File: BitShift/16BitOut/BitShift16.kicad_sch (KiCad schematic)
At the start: 7 parts, among them U1 74AHC595, U2 74AHC595

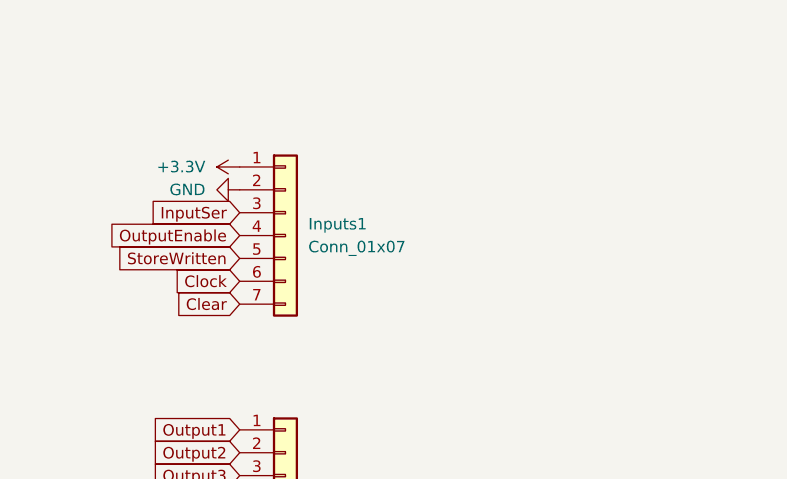
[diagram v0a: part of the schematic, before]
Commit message: renamed components
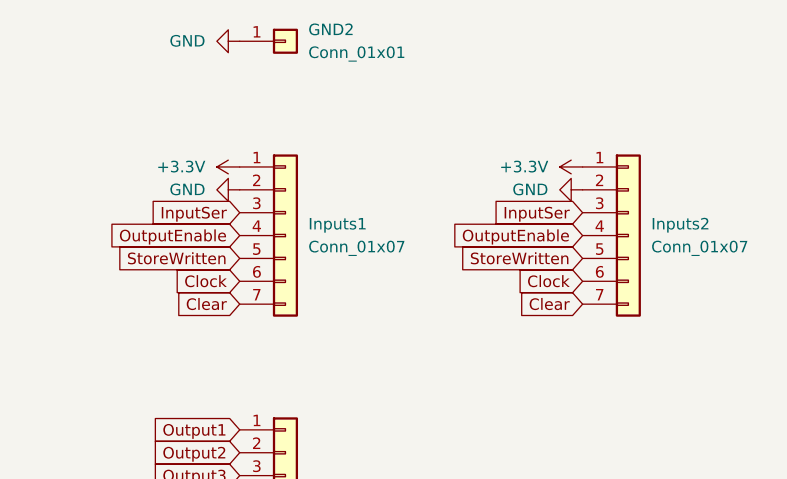
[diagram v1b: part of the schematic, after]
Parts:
- added GND2: Conn_01x01, Connector_PinHeader_2.54mm:PinHeader_1x01_P2.54mm_Vertical, symbol Connector_Generic:Conn_01x01
- added Inputs2: Conn_01x07, Connector_JST:JST_EH_S7B-EH_1x07_P2.50mm_Horizontal, symbol Connector_Generic:Conn_01x07
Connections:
- net +3.3V: now also Inputs2.1 (Pin_1)
- net Clear: now also Inputs2.7 (Pin_7)
- net Clock: now also Inputs2.6 (Pin_6)
- net GND: now also GND2.1 (Pin_1), Inputs2.2 (Pin_2)
- net InputSer: now also Inputs2.3 (Pin_3)
- net OutputEnable: now also Inputs2.4 (Pin_4)
- net StoreWritten: now also Inputs2.5 (Pin_5)
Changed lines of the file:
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@@
+    )
+  )
+  (global_label "Clear" (shape input) (at 257.81 86.36 180) (fields_autoplaced)
+    (effects (font (size 1.27 1.27)) (justify right))
+    (property "Intersheetrefs" "${INTERSHEET_REFS}" (at 249.8658 86.36 0)
+      (effects (font (size 1.27 1.27)) (justify right) hide)
     )
   )
@@
     )
   )
+  (global_label "Clock" (shape input) (at 257.81 83.82 180) (fields_autoplaced)
+    (effects (font (size 1.27 1.27)) (justify right))
+    (property "Intersheetrefs" "${INTERSHEET_REFS}" (at 249.6239 83.82 0)
+      (effects (font (size 1.27 1.27)) (justify right) hide)
+    )
+  )
   (global_label "Clock" (shape input) (at 219.71 83.82 180) (fields_autoplaced)
     (effects (font (size 1.27 1.27)) (justify right))
@@
     )
   )
+  (global_label "InputSer" (shape input) (at 257.81 76.2 180) (fields_autoplaced)
+    (effects (font (size 1.27 1.27)) (justify right))
+    (property "Intersheetrefs" "${INTERSHEET_REFS}" (at 246.963 76.2 0)
+      (effects (font (size 1.27 1.27)) (justify right) hide)
+    )
+  )
   (global_label "Output10" (shape input) (at 158.75 140.97 0) (fields_autoplaced)
     (effects (font (size 1.27 1.27)) (justify left))
@@
     )
   )
+  (global_label "StoreWritten" (shape input) (at 257.81 81.28 180) (fields_autoplaced)
+    (effects (font (size 1.27 1.27)) (justify right))
+    (property "Intersheetrefs" "${INTERSHEET_REFS}" (at 243.3344 81.28 0)
+      (effects (font (size 1.27 1.27)) (justify right) hide)
+    )
+  )
   (global_label "Clear" (shape input) (at 121.92 85.09 180) (fields_autoplaced)
     (effects (font (size 1.27 1.27)) (justify right))
@@
     (property "Intersheetrefs" "${INTERSHEET_REFS}" (at 169.1736 85.09 0)
       (effects (font (size 1.27 1.27)) (justify left) hide)
+    )
+  )
+  (global_label "OutputEnable" (shape input) (at 257.81 78.74 180) (fields_autoplaced)
+    (effects (font (size 1.27 1.27)) (justify right))
+    (property "Intersheetrefs" "${INTERSHEET_REFS}" (at 242.2461 78.74 0)
+      (effects (font (size 1.27 1.27)) (justify right) hide)
     )
   )
@@
         (path "/33c18695-af67-4dec-a71b-72e9af012bd4"
           (reference "#PWR03") (unit 1)
+        )
+      )
+    )
+  )
+  (symbol (lib_id "Connector_Generic:Conn_01x07") (at 262.89 78.74 0) (unit 1)
+    (in_bom yes) (on_board yes) (dnp no) (fields_autoplaced)
+    (property "Reference" "Inputs2" (at 265.43 77.47 0)
+      (effects (font (size 1.27 1.27)) (justify left))
+    )
+    (property "Value" "Conn_01x07" (at 265.43 80.01 0)
+      (effects (font (size 1.27 1.27)) (justify left))
+    )
+    (property "Footprint" "Connector_JST:JST_EH_S7B-EH_1x07_P2.50mm_Horizontal" (at 262.89 78.74 0)
+      (effects (font (size 1.27 1.27)) hide)
+    )
+    (property "Datasheet" "~" (at 262.89 78.74 0)
+      (effects (font (size 1.27 1.27)) hide)
+    )
+    (pin "6")
+    (pin "4")
+    (pin "7")
+    (pin "1")
+    (pin "3")
+    (pin "5")
+    (pin "2")
+    (instances
+      (project "MultiBitShift"
+        (path "/33c18695-af67-4dec-a71b-72e9af012bd4"
+          (reference "Inputs2") (unit 1)
         )
       )
@@
         (path "/33c18695-af67-4dec-a71b-72e9af012bd4"
           (reference "Outputs1") (unit 1)
+        )
+      )
+    )
+  )
+  (symbol (lib_id "power:+3.3V") (at 257.81 71.12 90) (unit 1)
+    (in_bom yes) (on_board yes) (dnp no) (fields_autoplaced)
+    (property "Reference" "#PWR08" (at 261.62 71.12 0)
+      (effects (font (size 1.27 1.27)) hide)
+    )
+    (property "Value" "+3.3V" (at 254 71.12 90)
+      (effects (font (size 1.27 1.27)) (justify left))
+    )
+    (property "Footprint" "" (at 257.81 71.12 0)
+      (effects (font (size 1.27 1.27)) hide)
+    )
+    (property "Datasheet" "" (at 257.81 71.12 0)
+      (effects (font (size 1.27 1.27)) hide)
+    )
+    (pin "1")
+    (instances
+      (project "MultiBitShift"
+        (path "/33c18695-af67-4dec-a71b-72e9af012bd4"
+          (reference "#PWR08") (unit 1)
+        )
+      )
+    )
+  )
+  (symbol (lib_id "power:GND") (at 219.71 57.15 270) (unit 1)
+    (in_bom yes) (on_board yes) (dnp no) (fields_autoplaced)
+    (property "Reference" "#PWR07" (at 213.36 57.15 0)
+      (effects (font (size 1.27 1.27)) hide)
+    )
+    (property "Value" "GND" (at 215.9 57.15 90)
+      (effects (font (size 1.27 1.27)) (justify right))
+    )
+    (property "Footprint" "" (at 219.71 57.15 0)
+      (effects (font (size 1.27 1.27)) hide)
+    )
+    (property "Datasheet" "" (at 219.71 57.15 0)
+      (effects (font (size 1.27 1.27)) hide)
+    )
+    (pin "1")
+    (instances
+      (project "MultiBitShift"
+        (path "/33c18695-af67-4dec-a71b-72e9af012bd4"
+          (reference "#PWR07") (unit 1)
+        )
+      )
+    )
+  )
+  (symbol (lib_id "power:GND") (at 257.81 73.66 270) (unit 1)
+    (in_bom yes) (on_board yes) (dnp no) (fields_autoplaced)
+    (property "Reference" "#PWR09" (at 251.46 73.66 0)
+      (effects (font (size 1.27 1.27)) hide)
+    )
+    (property "Value" "GND" (at 254 73.66 90)
+      (effects (font (size 1.27 1.27)) (justify right))
+    )
+    (property "Footprint" "" (at 257.81 73.66 0)
+      (effects (font (size 1.27 1.27)) hide)
+    )
+    (property "Datasheet" "" (at 257.81 73.66 0)
+      (effects (font (size 1.27 1.27)) hide)
+    )
+    (pin "1")
+    (instances
+      (project "MultiBitShift"
+        (path "/33c18695-af67-4dec-a71b-72e9af012bd4"
+          (reference "#PWR09") (unit 1)
         )
       )
@@
         )
       )
+    )
+  )
+  (symbol (lib_id "Connector_Generic:Conn_01x01") (at 224.79 57.15 0) (unit 1)
+    (in_bom yes) (on_board yes) (dnp no) (fields_autoplaced)
+    (property "Reference" "GND2" (at 227.33 55.88 0)
+      (effects (font (size 1.27 1.27)) (justify left))
+    )
+    (property "Value" "Conn_01x01" (at 227.33 58.42 0)
+      (effects (font (size 1.27 1.27)) (justify left))
+    )
+    (property "Footprint" "Connector_PinHeader_2.54mm:PinHeader_1x01_P2.54mm_Vertical" (at 224.79 57.15 0)
+      (effects (font (size 1.27 1.27)) hide)
+    )
+    (property "Datasheet" "~" (at 224.79 57.15 0)
+      (effects (font (size 1.27 1.27)) hide)
+    )
+    (pin "1")
+    (instances
+      (project "MultiBitShift"
+        (path "/33c18695-af67-4dec-a71b-72e9af012bd4"
+          (reference "GND2") (unit 1)
+        )
+      )
